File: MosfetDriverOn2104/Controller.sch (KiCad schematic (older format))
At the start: 23 parts

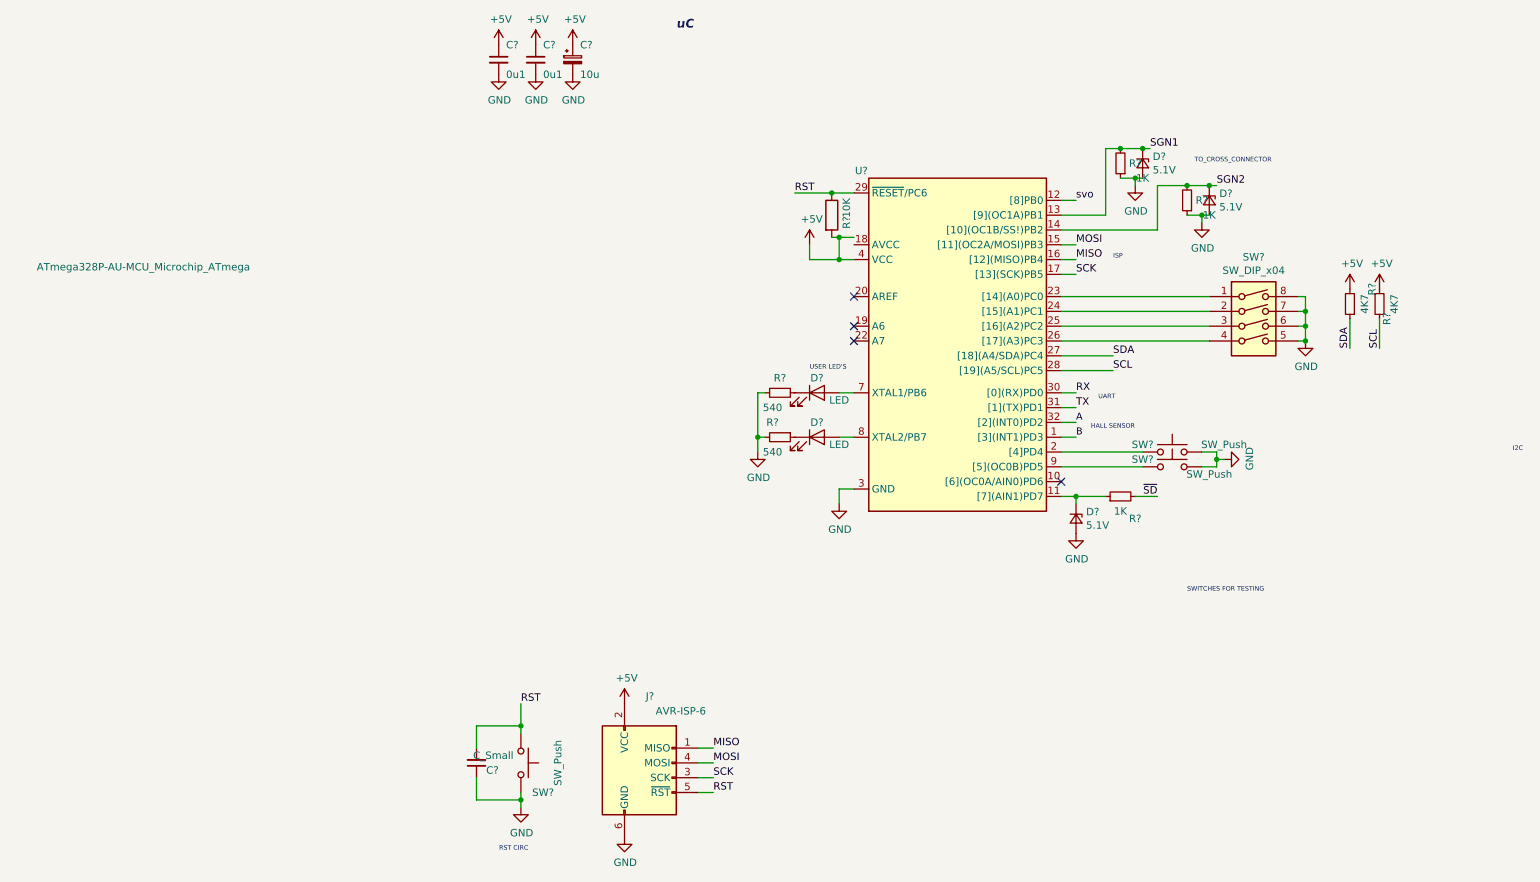
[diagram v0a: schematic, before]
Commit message: Completed Hirarcheial Sch, fixes #9
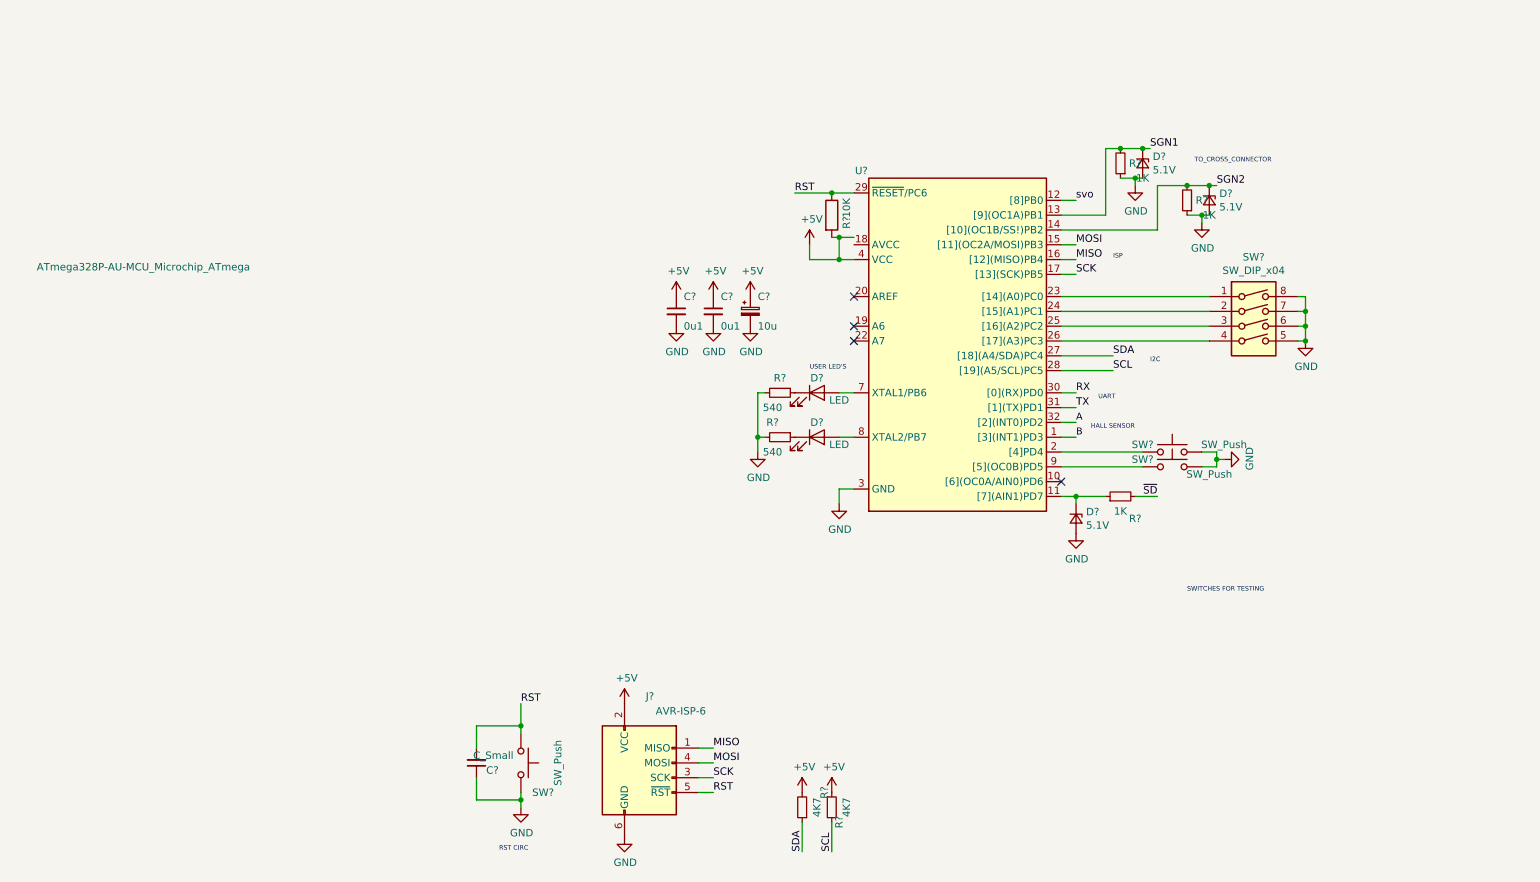
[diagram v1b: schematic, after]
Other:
- note removed: "uC"
- moved on the sheet: C?, R?
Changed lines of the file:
@@
 $Descr A4 11693 8268
 encoding utf-8
-Sheet 3 3
+Sheet 3 4
 Title ""
 Date ""
@@
 L power:+5V #PWR?
 U 1 1 5BD68DF0
-P 1450 1750
+P 2650 3450
 AR Path="/5BD68DF0" Ref="#PWR?"  Part="1"
 AR Path="/5BD66C24/5BD68DF0" Ref="#PWR?"  Part="1"
-F 0 "#PWR?" H 1450 1600 50  0001 C CNN
-F 1 "+5V" H 1465 1923 50  0000 C CNN
-F 2 "" H 1450 1750 50  0001 C CNN
-F 3 "" H 1450 1750 50  0001 C CNN
-	1    1450 1750
+F 0 "#PWR?" H 2650 3300 50  0001 C CNN
+F 1 "+5V" H 2665 3623 50  0000 C CNN
+F 2 "" H 2650 3450 50  0001 C CNN
+F 3 "" H 2650 3450 50  0001 C CNN
+	1    2650 3450
 	1    0    0    -1
 $EndComp
@@
 L power:GND #PWR?
 U 1 1 5BD68DF6
-P 1450 1950
+P 2650 3650
 AR Path="/5BD68DF6" Ref="#PWR?"  Part="1"
 AR Path="/5BD66C24/5BD68DF6" Ref="#PWR?"  Part="1"
-F 0 "#PWR?" H 1450 1700 50  0001 C CNN
-F 1 "GND" H 1455 1777 50  0000 C CNN
-F 2 "" H 1450 1950 50  0001 C CNN
-F 3 "" H 1450 1950 50  0001 C CNN
-	1    1450 1950
+F 0 "#PWR?" H 2650 3400 50  0001 C CNN
+F 1 "GND" H 2655 3477 50  0000 C CNN
+F 2 "" H 2650 3650 50  0001 C CNN
+F 3 "" H 2650 3650 50  0001 C CNN
+	1    2650 3650
 	1    0    0    -1
 $EndComp
@@
 L Device:C_Small C?
 U 1 1 5BD68E03
-P 1200 1850
+P 2400 3550
 AR Path="/5BD68E03" Ref="C?"  Part="1"
 AR Path="/5BD66C24/5BD68E03" Ref="C?"  Part="1"
-F 0 "C?" H 1250 1950 50  0000 L CNN
-F 1 "0u1" H 1250 1750 50  0000 L CNN
-F 2 "Capacitor_SMD:C_0805_2012Metric" H 1200 1850 50  0001 C CNN
-F 3 "~" H 1200 1850 50  0001 C CNN
-	1    1200 1850
+F 0 "C?" H 2450 3650 50  0000 L CNN
+F 1 "0u1" H 2450 3450 50  0000 L CNN
+F 2 "Capacitor_SMD:C_0805_2012Metric" H 2400 3550 50  0001 C CNN
+F 3 "~" H 2400 3550 50  0001 C CNN
+	1    2400 3550
 	1    0    0    -1
 $EndComp
@@
 L Device:C_Small C?
 U 1 1 5BD68E0A
-P 1450 1850
+P 2650 3550
 AR Path="/5BD68E0A" Ref="C?"  Part="1"
 AR Path="/5BD66C24/5BD68E0A" Ref="C?"  Part="1"
-F 0 "C?" H 1500 1950 50  0000 L CNN
-F 1 "0u1" H 1500 1750 50  0000 L CNN
-F 2 "Capacitor_SMD:C_0805_2012Metric" H 1450 1850 50  0001 C CNN
-F 3 "~" H 1450 1850 50  0001 C CNN
-	1    1450 1850
+F 0 "C?" H 2700 3650 50  0000 L CNN
+F 1 "0u1" H 2700 3450 50  0000 L CNN
+F 2 "Capacitor_SMD:C_0805_2012Metric" H 2650 3550 50  0001 C CNN
+F 3 "~" H 2650 3550 50  0001 C CNN
+	1    2650 3550
 	1    0    0    -1
 $EndComp
@@
 L Device:CP_Small C?
 U 1 1 5BD68E11
-P 1700 1850
+P 2900 3550
 AR Path="/5BD68E11" Ref="C?"  Part="1"
 AR Path="/5BD66C24/5BD68E11" Ref="C?"  Part="1"
-F 0 "C?" H 1750 1950 50  0000 L CNN
-F 1 "10u" H 1750 1750 50  0000 L CNN
-F 2 "Capacitor_SMD:CP_Elec_5x4.4" H 1700 1850 50  0001 C CNN
-F 3 "~" H 1700 1850 50  0001 C CNN
-	1    1700 1850
+F 0 "C?" H 2950 3650 50  0000 L CNN
+F 1 "10u" H 2950 3450 50  0000 L CNN
+F 2 "Capacitor_SMD:CP_Elec_5x4.4" H 2900 3550 50  0001 C CNN
+F 3 "~" H 2900 3550 50  0001 C CNN
+	1    2900 3550
 	1    0    0    -1
 $EndComp
@@
 Wire Wire Line
 	5100 4100 5000 4100
-Text Label 6950 3800 1    50   ~ 0
+Text Label 3250 7200 1    50   ~ 0
 SDA
-Text Label 7150 3800 1    50   ~ 0
+Text Label 3450 7200 1    50   ~ 0
 SCL
 $Comp
@@
 L Device:R_Small R?
 U 1 1 5BD68E5E
-P 6950 3500
+P 3250 6900
 AR Path="/5BD68E5E" Ref="R?"  Part="1"
 AR Path="/5BD66C24/5BD68E5E" Ref="R?"  Part="1"
-F 0 "R?" V 6800 3400 50  0000 C CNN
-F 1 "4K7" V 6850 3500 50  0000 C CNN
-F 2 "Resistor_SMD:R_0805_2012Metric" H 6950 3500 50  0001 C CNN
-F 3 "~" H 6950 3500 50  0001 C CNN
-	1    6950 3500
+F 0 "R?" V 3100 6800 50  0000 C CNN
+F 1 "4K7" V 3150 6900 50  0000 C CNN
+F 2 "Resistor_SMD:R_0805_2012Metric" H 3250 6900 50  0001 C CNN
+F 3 "~" H 3250 6900 50  0001 C CNN
+	1    3250 6900
 	-1   0    0    1
 $EndComp
@@
 L Device:R_Small R?
 U 1 1 5BD68E65
-P 7150 3500
+P 3450 6900
 AR Path="/5BD68E65" Ref="R?"  Part="1"
 AR Path="/5BD66C24/5BD68E65" Ref="R?"  Part="1"
-F 0 "R?" V 7200 3400 50  0000 C CNN
-F 1 "4K7" V 7250 3500 50  0000 C CNN
-F 2 "Resistors_SMD:R_0805" H 7150 3500 50  0001 C CNN
-F 3 "~" H 7150 3500 50  0001 C CNN
-	1    7150 3500
+F 0 "R?" V 3500 6800 50  0000 C CNN
+F 1 "4K7" V 3550 6900 50  0000 C CNN
+F 2 "Resistors_SMD:R_0805" H 3450 6900 50  0001 C CNN
+F 3 "~" H 3450 6900 50  0001 C CNN
+	1    3450 6900
 	1    0    0    -1
 $EndComp
@@
 Wire Wire Line
 	5000 3000 5650 3000
-Text Notes 2400 1650 0    59   Italic 12
-uC
 Wire Wire Line
 	5550 2650 5500 2650
@@
 Text Notes 5250 4150 0    31   ~ 0
 UART\n
-Text Notes 8050 4500 0    31   ~ 0
+Text Notes 5600 3900 0    31   ~ 0
 I2C\n
 Text Notes 5850 5450 0    31   ~ 0
@@
 L power:+5V #PWR?
 U 1 1 5BD75D62
-P 1200 1750
+P 2400 3450
 AR Path="/5BD75D62" Ref="#PWR?"  Part="1"
 AR Path="/5BD66C24/5BD75D62" Ref="#PWR?"  Part="1"
-F 0 "#PWR?" H 1200 1600 50  0001 C CNN
-F 1 "+5V" H 1215 1923 50  0000 C CNN
-F 2 "" H 1200 1750 50  0001 C CNN
-F 3 "" H 1200 1750 50  0001 C CNN
-	1    1200 1750
+F 0 "#PWR?" H 2400 3300 50  0001 C CNN
+F 1 "+5V" H 2415 3623 50  0000 C CNN
+F 2 "" H 2400 3450 50  0001 C CNN
+F 3 "" H 2400 3450 50  0001 C CNN
+	1    2400 3450
 	1    0    0    -1
 $EndComp
@@
 L power:+5V #PWR?
 U 1 1 5BD75DEA
-P 1700 1750
+P 2900 3450
 AR Path="/5BD75DEA" Ref="#PWR?"  Part="1"
 AR Path="/5BD66C24/5BD75DEA" Ref="#PWR?"  Part="1"
-F 0 "#PWR?" H 1700 1600 50  0001 C CNN
-F 1 "+5V" H 1715 1923 50  0000 C CNN
-F 2 "" H 1700 1750 50  0001 C CNN
-F 3 "" H 1700 1750 50  0001 C CNN
-	1    1700 1750
+F 0 "#PWR?" H 2900 3300 50  0001 C CNN
+F 1 "+5V" H 2915 3623 50  0000 C CNN
+F 2 "" H 2900 3450 50  0001 C CNN
+F 3 "" H 2900 3450 50  0001 C CNN
+	1    2900 3450
 	1    0    0    -1
 $EndComp
@@
 L power:GND #PWR?
 U 1 1 5BD75E23
-P 1200 1950
+P 2400 3650
 AR Path="/5BD75E23" Ref="#PWR?"  Part="1"
 AR Path="/5BD66C24/5BD75E23" Ref="#PWR?"  Part="1"
-F 0 "#PWR?" H 1200 1700 50  0001 C CNN
-F 1 "GND" H 1205 1777 50  0000 C CNN
-F 2 "" H 1200 1950 50  0001 C CNN
-F 3 "" H 1200 1950 50  0001 C CNN
-	1    1200 1950
+F 0 "#PWR?" H 2400 3400 50  0001 C CNN
+F 1 "GND" H 2405 3477 50  0000 C CNN
+F 2 "" H 2400 3650 50  0001 C CNN
+F 3 "" H 2400 3650 50  0001 C CNN
+	1    2400 3650
 	1    0    0    -1
 $EndComp
@@
 L power:GND #PWR?
 U 1 1 5BD75E5C
-P 1700 1950
+P 2900 3650
 AR Path="/5BD75E5C" Ref="#PWR?"  Part="1"
 AR Path="/5BD66C24/5BD75E5C" Ref="#PWR?"  Part="1"
-F 0 "#PWR?" H 1700 1700 50  0001 C CNN
-F 1 "GND" H 1705 1777 50  0000 C CNN
-F 2 "" H 1700 1950 50  0001 C CNN
-F 3 "" H 1700 1950 50  0001 C CNN
-	1    1700 1950
+F 0 "#PWR?" H 2900 3400 50  0001 C CNN
+F 1 "GND" H 2905 3477 50  0000 C CNN
+F 2 "" H 2900 3650 50  0001 C CNN
+F 3 "" H 2900 3650 50  0001 C CNN
+	1    2900 3650
 	1    0    0    -1
 $EndComp
@@
 L power:+5V #PWR?
 U 1 1 5BD68E6E
-P 7150 3400
+P 3450 6800
 AR Path="/5BD68E6E" Ref="#PWR?"  Part="1"
 AR Path="/5BD66C24/5BD68E6E" Ref="#PWR?"  Part="1"
-F 0 "#PWR?" H 7150 3250 50  0001 C CNN
-F 1 "+5V" H 7165 3573 50  0000 C CNN
-F 2 "" H 7150 3400 50  0001 C CNN
-F 3 "" H 7150 3400 50  0001 C CNN
-	1    7150 3400
+F 0 "#PWR?" H 3450 6650 50  0001 C CNN
+F 1 "+5V" H 3465 6973 50  0000 C CNN
+F 2 "" H 3450 6800 50  0001 C CNN
+F 3 "" H 3450 6800 50  0001 C CNN
+	1    3450 6800
 	1    0    0    -1
 $EndComp
@@
 L power:+5V #PWR?
 U 1 1 5BDD9EFE
-P 6950 3400
+P 3250 6800
 AR Path="/5BDD9EFE" Ref="#PWR?"  Part="1"
 AR Path="/5BD66C24/5BDD9EFE" Ref="#PWR?"  Part="1"
-F 0 "#PWR?" H 6950 3250 50  0001 C CNN
-F 1 "+5V" H 6965 3573 50  0000 C CNN
-F 2 "" H 6950 3400 50  0001 C CNN
-F 3 "" H 6950 3400 50  0001 C CNN
-	1    6950 3400
-	1    0    0    -1
-$EndComp
-Wire Wire Line
-	6950 3800 6950 3600
-Wire Wire Line
-	7150 3800 7150 3600
+F 0 "#PWR?" H 3250 6650 50  0001 C CNN
+F 1 "+5V" H 3265 6973 50  0000 C CNN
+F 2 "" H 3250 6800 50  0001 C CNN
+F 3 "" H 3250 6800 50  0001 C CNN
+	1    3250 6800
+	1    0    0    -1
+$EndComp
+Wire Wire Line
+	3250 7200 3250 7000
+Wire Wire Line
+	3450 7200 3450 7000
 $EndSCHEMATC
